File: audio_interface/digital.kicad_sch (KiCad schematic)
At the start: 33 parts

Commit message: Further changes
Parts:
- removed J?: INST_EXT, symbol Connector_Generic:Conn_01x01
- removed J?: MIC_EXT, symbol Connector_Generic:Conn_01x01
- removed JP? (x6): Jumper_2_Bridged, symbol Jumper:Jumper_2_Bridged
- removed U?: STM32F042T6Yx, Package_CSP:ST_WLCSP-36_Die445, symbol MCU_ST_STM32F0:STM32F042T6Yx
- added C44, C45, C46, C47: 100n, symbol Device:C
- added D10: CLIP_I, symbol Device:LED
- added D5, D6, D7, D8: D_Schottky, symbol Device:D_Schottky
- added D9: CLIP_M, symbol Device:LED
- added J11: Test Headers, symbol Connector_Generic:Conn_01x04
- added J12: SWD, symbol Connector_Generic:Conn_01x06
- added J13: USB_B, symbol Connector:USB_B
- added J8: MIC_EXT, symbol Connector_Generic:Conn_01x02
- added J9: INST_EXT, symbol Connector_Generic:Conn_01x02
- added JP19, JP20, JP29, JP34, JP35, JP36, JP37, JP38, JP39, JP40, JP41, JP42: Jumper_2_Bridged, symbol Jumper:Jumper_2_Bridged
- added R27, R28: 250, symbol Device:R_US
- added SW1: SW_Push, symbol Switch:SW_Push
- added U10: STM32F042K6Tx, Package_QFP:LQFP-32_7x7mm_P0.8mm, symbol MCU_ST_STM32F0:STM32F042K6Tx
- gave numbers to parts that had none: 24
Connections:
- net +3V3: now also J12.1 (Pin_1), JP19.1 (A), JP35.2 (B)
- net +5V: now also D5.1 (K), D7.1 (K), JP34.2 (B); no longer C41.1, C43.1, U9.22 (Vcc)
- net 2V5A_I: now also J9.2 (Pin_2)
- net 2V5A_M: now also J8.2 (Pin_2)
- net CLIP_L: now also JP36.2 (B)
- net CLIP_R: now also JP37.2 (B)
- net GNDA: now also D6.2 (A), D8.2 (A)
- net GNDD: now also C44.2, C45.2, C46.2, C47.2, D10.1 (K), D9.1 (K), J13.4 (GND), J13.5 (Shield), SW1.2, U10.16 (VSS), U10.32 (VSSA)
- net I2S_CLK: now also U9.16 (BCK), JP41.2 (B)
- net I2S_SD: now also U9.15 (DATA), JP42.2 (B)
- net I2S_WS: now also U9.17 (LRCK), JP40.2 (B)
- net INST_OUT: now also JP29.1 (A)
- net MIC_OUT: now also JP20.1 (A)
- net PCM_CLK: now also U9.18 (SCKI), JP39.2 (B)
- net PCM_RST_n: now also JP38.2 (B)
- net USB_DM: now also J13.2 (D-), U10.21 (PA11)
- net USB_DP: now also J13.3 (D+), U10.22 (PA12)
- net at C37.1, C39.1, U9.14 (Vdd): now also JP19.2 (B)
- net INST_ADC: now reaches U9.25 (Vin_R+)
- net INST_ADC: now also D7.2 (A), D8.1 (K), J9.1 (Pin_1), JP29.2 (B)
- net MIC_ADC: now reaches U9.4 (Vin_L+)
- net MIC_ADC: now also D5.2 (A), D6.1 (K), J8.1 (Pin_1), JP20.2 (B)
- new net: C41.1, C43.1, JP34.1 (A), U9.22 (Vcc)
- new net: D9.2 (A), R27.2
- new net: C44.1, C45.1, C46.1, JP35.1 (A), U10.1 (VDD), U10.17 (VDDIO2), U10.5 (VDDA)
- new net: D10.2 (A), R28.2
- new net: J12.4 (Pin_4), U10.23 (PA13)
- new net: J12.2 (Pin_2), U10.24 (PA14)
- new net: R27.1, U10.30 (PB7)
- new net: R28.1, U10.31 (PB8)
- new net: J11.1 (Pin_1), U10.6 (PA0)
- new net: J11.2 (Pin_2), U10.7 (PA1)
- new net: J11.3 (Pin_3), U10.8 (PA2)
- new net: J11.4 (Pin_4), U10.9 (PA3)
- new net GND: J12.3 (Pin_3)
- new net RST_n: C47.1, J12.5 (Pin_5), SW1.1, U10.4 (NRST)
- new net STM_CLIP_L: JP36.1 (A), U10.18 (PA8)
- new net STM_CLIP_R: JP37.1 (A), U10.19 (PA9)
- new net STM_I2S_CLK: JP41.1 (A), U10.11 (PA5)
- new net STM_I2S_SD: JP42.1 (A), U10.13 (PA7)
- new net STM_I2S_WS: JP40.1 (A), U10.10 (PA4)
- new net STM_PCM_CLK: JP39.1 (A), U10.12 (PA6)
- new net STM_PCM_RST_n: JP38.1 (A), U10.20 (PA10)
- new net USB_5V: J13.1 (VBUS)
- no-connect marks 0 -> 1
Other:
- note added: "Schottkys <0.3v drop"
- note added: "UART"
- note added: "VDD_TARGET SWCLK GND SWDIO NRST SWO"

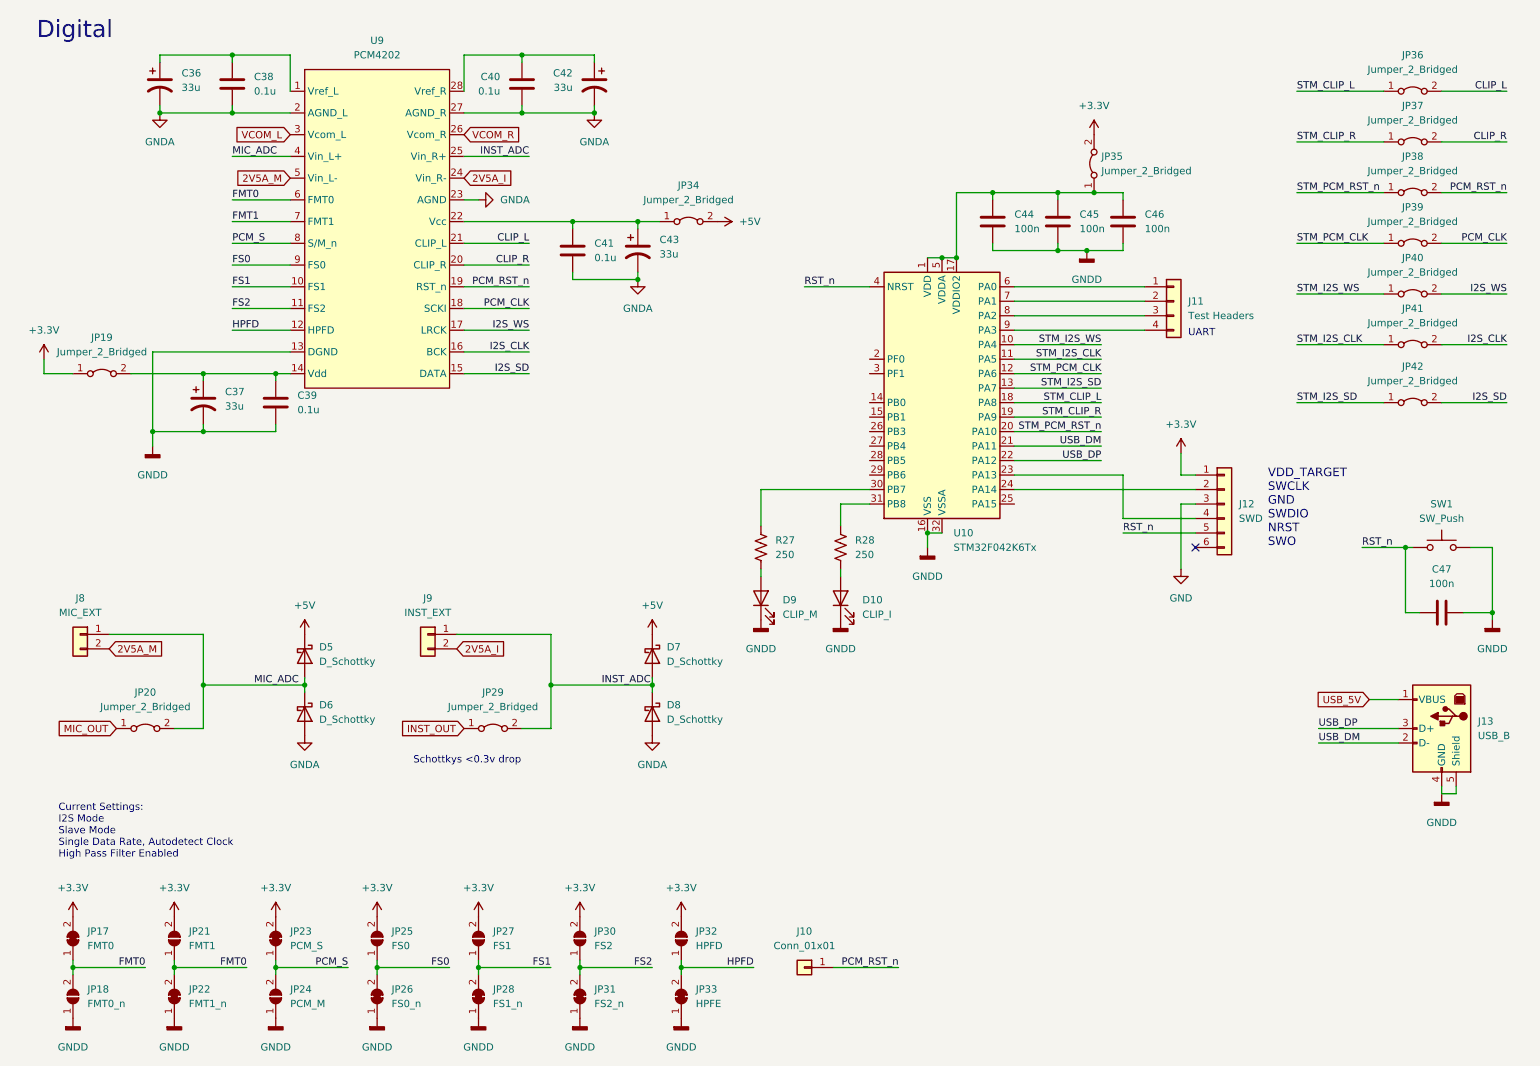
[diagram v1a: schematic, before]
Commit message: Added TP and fixed some capacitor values after SPICE sim.
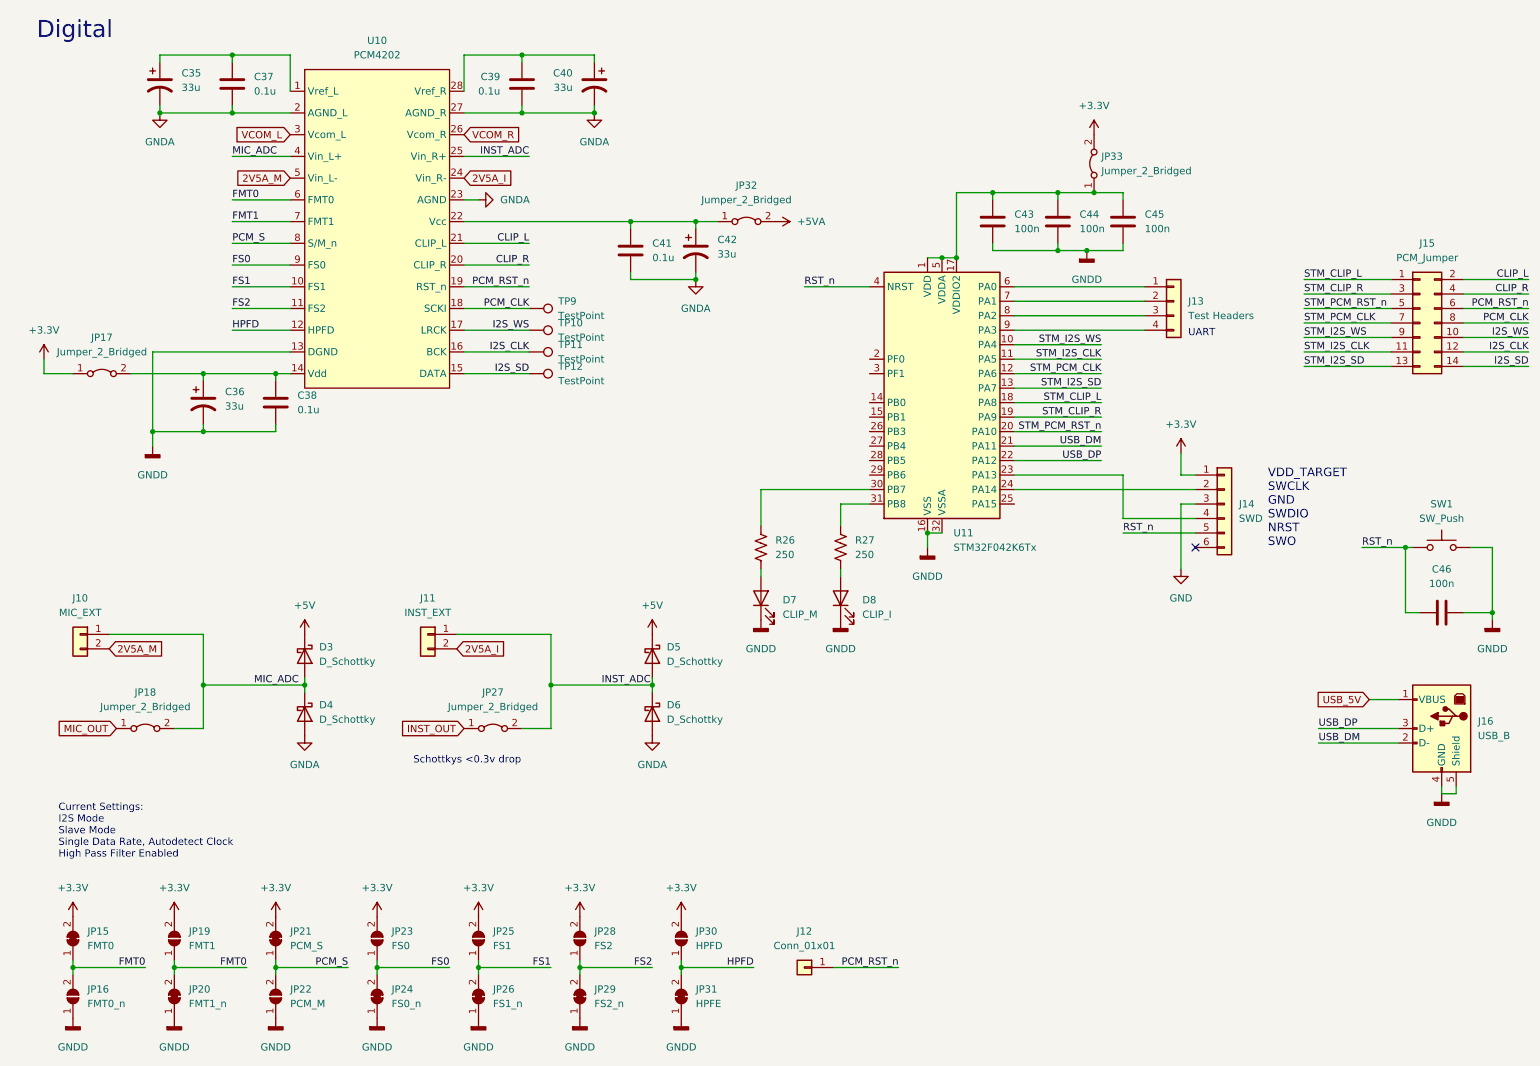
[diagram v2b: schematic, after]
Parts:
- removed JP36, JP37, JP38, JP39, JP40, JP41, JP42: Jumper_2_Bridged, symbol Jumper:Jumper_2_Bridged
- added J15: PCM_Jumper, symbol Connector_Generic:Conn_02x07_Odd_Even
- added TP10, TP11, TP12, TP9: TestPoint, symbol Connector:TestPoint
- renumbered C36 to C35, C37 to C36, C38 to C37, C39 to C38, C40 to C39, C42 to C40, C43 to C42, C44 to C43, C45 to C44, C46 to C45, C47 to C46, D5 to D3, D6 to D4, D7 to D5, D8 to D6, D9 to D7, D10 to D8, J8 to J10, J9 to J11, J10 to J12, J11 to J13, J12 to J14, J13 to J16, JP17 to JP15, JP18 to JP16, JP19 to JP17, JP20 to JP18, JP21 to JP19, JP22 to JP20, JP23 to JP21, JP24 to JP22, JP25 to JP23, JP26 to JP24, JP27 to JP25, JP28 to JP26, JP29 to JP27, JP30 to JP28, JP31 to JP29, JP32 to JP30, JP33 to JP31, JP34 to JP32, JP35 to JP33, R27 to R26, R28 to R27, U9 to U10, U10 to U11
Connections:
- net +5V: no longer JP32.2 (B)
- net CLIP_L: now also J15.2 (Pin_2)
- net CLIP_R: now also J15.4 (Pin_4)
- net I2S_CLK: now also J15.12 (Pin_12), TP11.1
- net I2S_SD: now also J15.14 (Pin_14), TP12.1
- net I2S_WS: now also J15.10 (Pin_10), TP10.1
- net PCM_CLK: now also J15.8 (Pin_8), TP9.1
- net PCM_RST_n: now also J15.6 (Pin_6)
- net STM_CLIP_L: now also J15.1 (Pin_1)
- net STM_CLIP_R: now also J15.3 (Pin_3)
- net STM_I2S_CLK: now also J15.11 (Pin_11)
- net STM_I2S_SD: now also J15.13 (Pin_13)
- net STM_I2S_WS: now also J15.9 (Pin_9)
- net STM_PCM_CLK: now also J15.7 (Pin_7)
- net STM_PCM_RST_n: now also J15.5 (Pin_5)
- new net +5VA: JP32.2 (B)
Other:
- moved on the sheet: C41, C42, JP32

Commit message: Added some footprints.
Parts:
- removed JP15: FMT0, symbol Jumper:SolderJumper_2_Bridged
- removed JP16: FMT0_n, symbol Jumper:SolderJumper_2_Open
- removed JP19: FMT1, symbol Jumper:SolderJumper_2_Open
- removed JP20: FMT1_n, symbol Jumper:SolderJumper_2_Bridged
- removed JP21: PCM_S, symbol Jumper:SolderJumper_2_Bridged
- removed JP22: PCM_M, symbol Jumper:SolderJumper_2_Open
- removed JP23: FS0, symbol Jumper:SolderJumper_2_Open
- removed JP24: FS0_n, symbol Jumper:SolderJumper_2_Bridged
- removed JP25: FS1, symbol Jumper:SolderJumper_2_Open
- removed JP26: FS1_n, symbol Jumper:SolderJumper_2_Bridged
- removed JP28: FS2, symbol Jumper:SolderJumper_2_Open
- removed JP29: FS2_n, symbol Jumper:SolderJumper_2_Bridged
- removed JP30: HPFD, symbol Jumper:SolderJumper_2_Open
- removed JP31: HPFE, symbol Jumper:SolderJumper_2_Bridged
- added JP15, JP16, JP19, JP20, JP21, JP22, JP23: (no value), symbol Jumper:SolderJumper_3_Bridged12
- C38: renamed from C37; footprint (none) -> Capacitor_SMD:C_0805_2012Metric_Pad1.15x1.40mm_HandSolder
- C39: renamed from C38; footprint (none) -> Capacitor_SMD:C_0805_2012Metric_Pad1.15x1.40mm_HandSolder
- C40: renamed from C39; footprint (none) -> Capacitor_SMD:C_0805_2012Metric_Pad1.15x1.40mm_HandSolder
- C42: renamed from C41; footprint (none) -> Capacitor_SMD:C_0805_2012Metric_Pad1.15x1.40mm_HandSolder
- C44: renamed from C43; value 100n -> 0.1u; footprint (none) -> Capacitor_SMD:C_0805_2012Metric_Pad1.15x1.40mm_HandSolder
- C45: renamed from C44; value 100n -> 0.1u; footprint (none) -> Capacitor_SMD:C_0805_2012Metric_Pad1.15x1.40mm_HandSolder
- C46: renamed from C45; value 100n -> 0.1u; footprint (none) -> Capacitor_SMD:C_0805_2012Metric_Pad1.15x1.40mm_HandSolder
- C47: renamed from C46; value 100n -> 0.1u; footprint (none) -> Capacitor_SMD:C_0805_2012Metric_Pad1.15x1.40mm_HandSolder
- JP17, JP18, JP27, JP32, JP33, R26, R27: footprint (none) -> Resistor_SMD:R_1206_3216Metric_Pad1.42x1.75mm_HandSolder
- TP10, TP11, TP12, TP9: footprint (none) -> TestPoint:TestPoint_Pad_1.5x1.5mm
- renumbered C35 to C36, C36 to C37, C40 to C41, C42 to C43
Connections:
- net +3V3: now also JP15.1 (A), JP16.3 (B), JP19.1 (A), JP20.3 (B), JP21.3 (B), JP22.3 (B), JP23.3 (B)
- net FMT0: now also JP15.2 (C)
- net FMT1: now also JP16.2 (C)
- net FS0: now also JP20.2 (C)
- net FS1: now also JP21.2 (C)
- net FS2: now also JP22.2 (C)
- net GNDD: now also JP15.3 (B), JP16.1 (A), JP19.3 (B), JP20.1 (A), JP21.1 (A), JP22.1 (A), JP23.1 (A)
- net HPFD: now also JP23.2 (C)
- net PCM_S: now also JP19.2 (C)
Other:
- moved on the sheet: J12

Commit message: Finished footprints.
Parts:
- C36, C37, C41, C43: footprint (none) -> Capacitor_SMD:CP_Elec_6.3x5.2
- C38, C39, C40, C42, C44, C45, C46, C47: footprint Capacitor_SMD:C_0805_2012Metric_Pad1.15x1.40mm_HandSolder -> Capacitor_SMD:C_0805_2012Metric_Pad1.18x1.45mm_HandSolder
- D3, D4, D5, D6: footprint (none) -> Diode_SMD:D_1206_3216Metric_Pad1.42x1.75mm_HandSolder
- D7, D8: footprint (none) -> LED_SMD:LED_1206_3216Metric_Pad1.42x1.75mm_HandSolder
- J10, J11: footprint (none) -> Connector_PinHeader_2.54mm:PinHeader_1x02_P2.54mm_Vertical
- J12: footprint (none) -> Connector_PinHeader_2.54mm:PinHeader_1x01_P2.54mm_Vertical
- J13: footprint (none) -> Connector_PinHeader_2.54mm:PinHeader_1x04_P2.54mm_Vertical
- J14: footprint (none) -> Connector_PinHeader_2.54mm:PinHeader_1x06_P2.54mm_Vertical
- J15: footprint (none) -> Connector_PinHeader_2.54mm:PinHeader_2x07_P2.54mm_Vertical
- J16: footprint (none) -> Connector_USB:USB_B_Lumberg_2411_02_Horizontal
- JP15: value (none) -> FMT0; footprint (none) -> Jumper:SolderJumper-3_P1.3mm_Open_RoundedPad1.0x1.5mm_NumberLabels
- JP16: value (none) -> FMT1_n; footprint (none) -> Jumper:SolderJumper-3_P1.3mm_Open_RoundedPad1.0x1.5mm_NumberLabels
- JP17, JP18, JP27, JP32, JP33, R26, R27: footprint Resistor_SMD:R_1206_3216Metric_Pad1.42x1.75mm_HandSolder -> Resistor_SMD:R_1206_3216Metric_Pad1.30x1.75mm_HandSolder
- JP19: value (none) -> PCM_S; footprint (none) -> Jumper:SolderJumper-3_P1.3mm_Open_RoundedPad1.0x1.5mm_NumberLabels
- JP20: value (none) -> FS0_n; footprint (none) -> Jumper:SolderJumper-3_P1.3mm_Open_RoundedPad1.0x1.5mm_NumberLabels
- JP21: value (none) -> FS1_n; footprint (none) -> Jumper:SolderJumper-3_P1.3mm_Open_RoundedPad1.0x1.5mm_NumberLabels
- JP22: value (none) -> FS2_n; footprint (none) -> Jumper:SolderJumper-3_P1.3mm_Open_RoundedPad1.0x1.5mm_NumberLabels
- JP23: value (none) -> HPFD_n; footprint (none) -> Jumper:SolderJumper-3_P1.3mm_Open_RoundedPad1.0x1.5mm_NumberLabels
- SW1: footprint (none) -> Button_Switch_THT:SW_PUSH_6mm
- U10: footprint (none) -> Package_SO:SSOP-28_5.3x10.2mm_P0.65mm

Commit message: Orion's layout
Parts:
- removed J12: Conn_01x01, Connector_PinHeader_2.54mm:PinHeader_1x01_P2.54mm_Vertical, symbol Connector_Generic:Conn_01x01
- D7, D8: footprint LED_SMD:LED_1206_3216Metric_Pad1.42x1.75mm_HandSolder -> LED_THT:LED_D3.0mm
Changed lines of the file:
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@@
-    (stroke (width 0) (type default) (color 0 0 0 0))
-  )
-  (wire (pts (xy 184.15 156.21) (xy 195.58 156.21))
     (stroke (width 0) (type default) (color 0 0 0 0))
   )
@@
   (label "MIC_ADC" (at 48.26 38.1 0)
     (effects (font (size 1.27 1.27)) (justify left bottom))
-  )
-  (label "PCM_RST_n" (at 195.58 156.21 180)
-    (effects (font (size 1.27 1.27)) (justify right bottom))
   )
   (label "FS0" (at 105.41 180.34 180)
@@
     (pin "1")
   )
-  (symbol (lib_id "Connector_Generic:Conn_01x01") (at 179.07 156.21 0) (mirror y) (unit 1)
-    (in_bom yes) (on_board yes) (fields_autoplaced)
-    (property "Reference" "J12" (id 0) (at 179.07 149.86 0))
-    (property "Value" "Conn_01x01" (id 1) (at 179.07 152.4 0))
-    (property "Footprint" "Connector_PinHeader_2.54mm:PinHeader_1x01_P2.54mm_Vertical" (id 2) (at 179.07 156.21 0)
-      (effects (font (size 1.27 1.27)) hide)
-    )
-    (property "Datasheet" "~" (id 3) (at 179.07 156.21 0)
-      (effects (font (size 1.27 1.27)) hide)
-    )
-    (pin "1")
-  )
   (symbol (lib_id "power:GNDD") (at 43.18 189.23 0) (unit 1)
     (in_bom yes) (on_board yes) (fields_autoplaced)
@@
       (effects (font (size 1.27 1.27)) (justify right))
     )
-    (property "Footprint" "LED_SMD:LED_1206_3216Metric_Pad1.42x1.75mm_HandSolder" (id 2) (at 140.97 115.57 0)
+    (property "Footprint" "LED_THT:LED_D3.0mm" (id 2) (at 140.97 115.57 0)
       (effects (font (size 1.27 1.27)) hide)
     )
@@
       (effects (font (size 1.27 1.27)) (justify right))
     )
-    (property "Footprint" "LED_SMD:LED_1206_3216Metric_Pad1.42x1.75mm_HandSolder" (id 2) (at 154.94 115.57 0)
-      (effects (font (size 1.27 1.27)) hide)
-    )
+    (property "Footprint" "LED_THT:LED_D3.0mm" (id 2) (at 154.94 115.57 0)
+      (effects (font (size 1.27 1.27)) hide)
+    )
